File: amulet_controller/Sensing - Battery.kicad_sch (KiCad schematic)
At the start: 3 parts

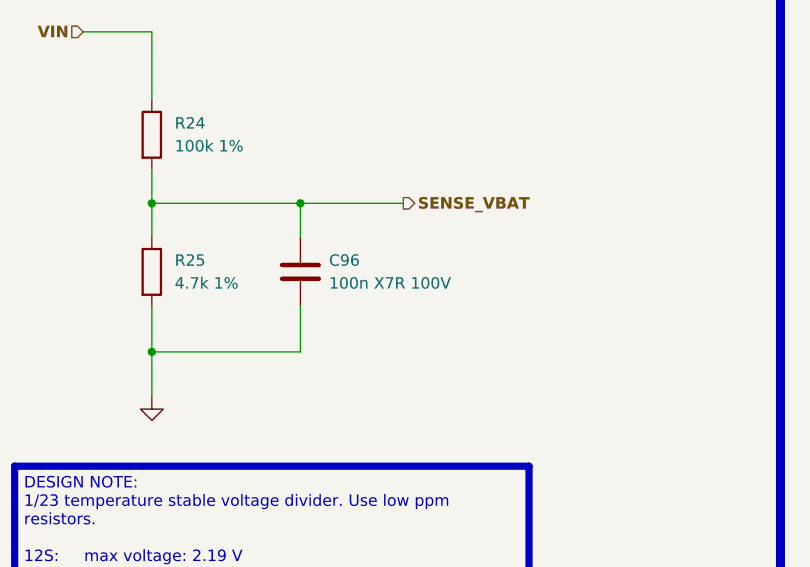
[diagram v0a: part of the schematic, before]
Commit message: filled in fields for bom, replaced inexisting components. Need to replace LEDs
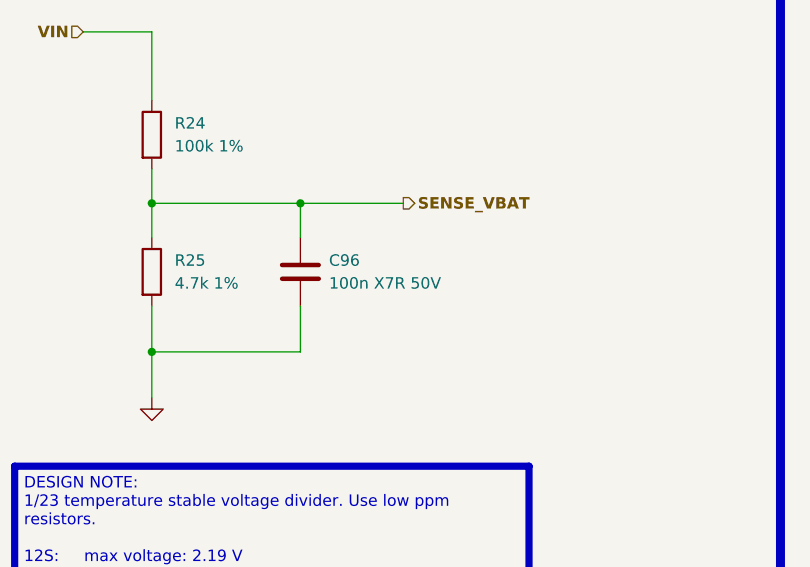
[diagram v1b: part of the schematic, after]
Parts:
- C96: value 100n X7R 100V -> 100n X7R 50V; Manufacturer (none) -> Murata Electronics; Manufacturer Part Number (none) -> GCM155R71H104KE02J; Supplier 1 (none) -> Digikey; Supplier Part Number 1 (none) -> 490-14514-1-ND
- R24: Manufacturer (none) -> YAGEO; Manufacturer Part Number (none) -> RT0402FRE07100KL; Supplier 1 (none) -> Digikey; Supplier Part Number 1 (none) -> YAG2307CT-ND
- R25: Manufacturer (none) -> YAGEO; Manufacturer Part Number (none) -> RT0402FRE134K7L; Supplier 1 (none) -> Digikey; Supplier Part Number 1 (none) -> 13-RT0402FRE134K7LCT-ND
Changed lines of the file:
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@@
       (effects (font (size 1.27 1.27)) hide)
     )
-    (property "Datasheet" "~" (at 134.62 78.74 0)
+    (property "Datasheet" "https://www.yageo.com/upload/media/product/app/datasheet/rchip/pyu-rt_1-to-0.01_rohs_l.pdf" (at 134.62 78.74 0)
+      (effects (font (size 1.27 1.27)) hide)
+    )
+    (property "Description" "RES 4.7K OHM 1% 1/16W 0402 50PPM" (at 134.62 78.74 0)
+      (effects (font (size 1.27 1.27)) hide)
+    )
+    (property "Manufacturer" "YAGEO" (at 134.62 78.74 0)
+      (effects (font (size 1.27 1.27)) hide)
+    )
+    (property "Manufacturer Part Number" "RT0402FRE134K7L" (at 134.62 78.74 0)
+      (effects (font (size 1.27 1.27)) hide)
+    )
+    (property "Supplier 1" "Digikey" (at 134.62 78.74 0)
+      (effects (font (size 1.27 1.27)) hide)
+    )
+    (property "Supplier Part Number 1" "13-RT0402FRE134K7LCT-ND" (at 134.62 78.74 0)
       (effects (font (size 1.27 1.27)) hide)
     )
@@
     (pin "2")
     (instances
-      (project "bldc_controller"
+      (project "amulet_controller"
         (path "/0650c7a8-acba-429c-9f8e-eec0baf0bc1c/fede4c36-00cc-4d3d-b71c-5243ba232202/5af28e14-08f4-4265-bd51-d6e5daa4b8a2"
           (reference "R25") (unit 1)
@@
       (effects (font (size 1.27 1.27)) (justify left))
     )
-    (property "Value" "100n X7R 100V" (at 154.305 80.01 0)
+    (property "Value" "100n X7R 50V" (at 154.305 80.01 0)
       (effects (font (size 1.27 1.27)) (justify left))
     )
@@
       (effects (font (size 1.27 1.27)) hide)
     )
-    (property "Datasheet" "~" (at 151.13 78.74 0)
+    (property "Datasheet" "https://search.murata.co.jp/Ceramy/image/img/A01X/G101/ENG/GCM155R71H104KE02-01.pdf" (at 151.13 78.74 0)
+      (effects (font (size 1.27 1.27)) hide)
+    )
+    (property "Description" "0.1 µF ±10% 50V Ceramic Capacitor X7R 0402 (1005 Metric)" (at 151.13 78.74 0)
+      (effects (font (size 1.27 1.27)) hide)
+    )
+    (property "Manufacturer" "Murata Electronics" (at 151.13 78.74 0)
+      (effects (font (size 1.27 1.27)) hide)
+    )
+    (property "Manufacturer Part Number" "GCM155R71H104KE02J" (at 151.13 78.74 0)
+      (effects (font (size 1.27 1.27)) hide)
+    )
+    (property "Supplier 1" "Digikey" (at 151.13 78.74 0)
+      (effects (font (size 1.27 1.27)) hide)
+    )
+    (property "Supplier Part Number 1" "490-14514-1-ND" (at 151.13 78.74 0)
       (effects (font (size 1.27 1.27)) hide)
     )
@@
     (pin "2")
     (instances
-      (project "bldc_controller"
+      (project "amulet_controller"
         (path "/0650c7a8-acba-429c-9f8e-eec0baf0bc1c/fede4c36-00cc-4d3d-b71c-5243ba232202/5af28e14-08f4-4265-bd51-d6e5daa4b8a2"
           (reference "C96") (unit 1)
@@
     (pin "1")
     (instances
-      (project "bldc_controller"
+      (project "amulet_controller"
         (path "/0650c7a8-acba-429c-9f8e-eec0baf0bc1c/fede4c36-00cc-4d3d-b71c-5243ba232202/5af28e14-08f4-4265-bd51-d6e5daa4b8a2"
           (reference "#PWR044") (unit 1)
@@
       (effects (font (size 1.27 1.27)) hide)
     )
-    (property "Datasheet" "~" (at 134.62 63.5 0)
+    (property "Datasheet" "https://www.yageo.com/upload/media/product/app/datasheet/rchip/pyu-rt_1-to-0.01_rohs_l.pdf" (at 134.62 63.5 0)
+      (effects (font (size 1.27 1.27)) hide)
+    )
+    (property "Description" "RES SMD 100K OHM 1% 1/16W 0402" (at 134.62 63.5 0)
+      (effects (font (size 1.27 1.27)) hide)
+    )
+    (property "Manufacturer" "YAGEO" (at 134.62 63.5 0)
+      (effects (font (size 1.27 1.27)) hide)
+    )
+    (property "Manufacturer Part Number" "RT0402FRE07100KL" (at 134.62 63.5 0)
+      (effects (font (size 1.27 1.27)) hide)
+    )
+    (property "Supplier 1" "Digikey" (at 134.62 63.5 0)
+      (effects (font (size 1.27 1.27)) hide)
+    )
+    (property "Supplier Part Number 1" "YAG2307CT-ND" (at 134.62 63.5 0)
       (effects (font (size 1.27 1.27)) hide)
     )
@@
     (pin "2")
     (instances
-      (project "bldc_controller"
+      (project "amulet_controller"
         (path "/0650c7a8-acba-429c-9f8e-eec0baf0bc1c/fede4c36-00cc-4d3d-b71c-5243ba232202/5af28e14-08f4-4265-bd51-d6e5daa4b8a2"
           (reference "R24") (unit 1)

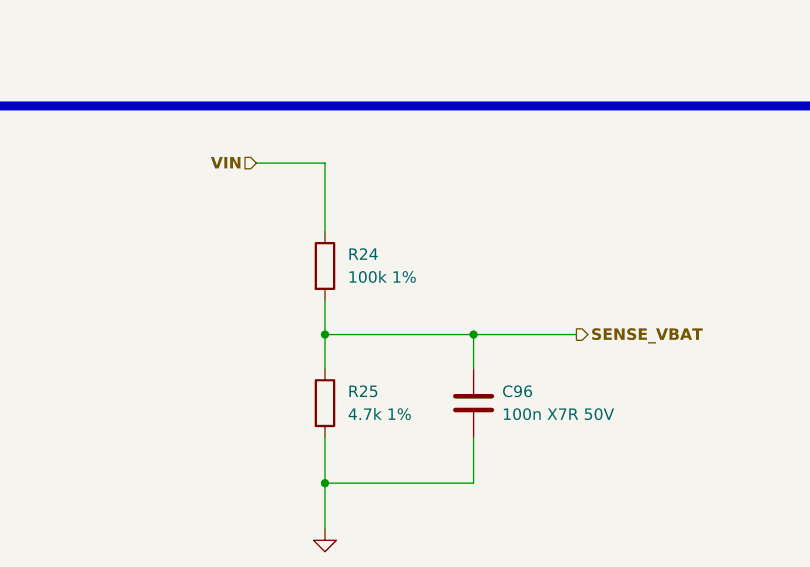
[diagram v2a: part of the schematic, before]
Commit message: finalized pcb. TODO: add clean BOM and KiBot integration
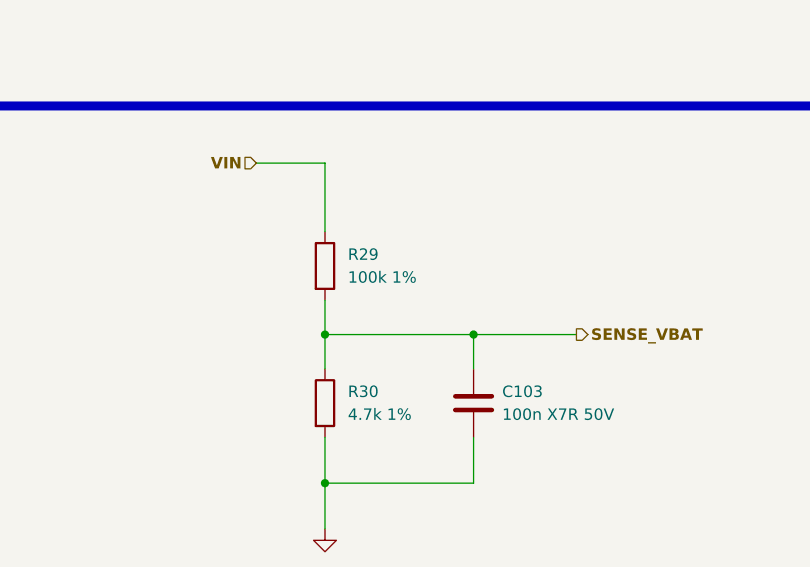
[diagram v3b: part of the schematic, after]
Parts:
- renumbered C96 to C103, R24 to R29, R25 to R30
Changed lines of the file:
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@@
+    (stroke (width 0) (type default))
+  )
+  (wire (pts (xy 134.62 59.69) (xy 134.62 52.07))
     (stroke (width 0) (type default))
   )
@@
     (stroke (width 0) (type default))
   )
-  (wire (pts (xy 134.62 52.07) (xy 134.62 59.69))
-    (stroke (width 0.381) (type default) (color 200 50 50 1))
+  (wire (pts (xy 151.13 71.12) (xy 162.56 71.12))
+    (stroke (width 0) (type default))
   )
-  (wire (pts (xy 151.13 71.12) (xy 162.56 71.12))
+  (wire (pts (xy 134.62 52.07) (xy 127 52.07))
     (stroke (width 0) (type default))
   )
   (wire (pts (xy 134.62 67.31) (xy 134.62 71.12))
     (stroke (width 0) (type default))
-  )
-  (wire (pts (xy 127 52.07) (xy 134.62 52.07))
-    (stroke (width 0.381) (type default) (color 200 50 50 1))
   )
   (wire (pts (xy 134.62 92.71) (xy 134.62 87.63))
@@
   )
   (hierarchical_label "VIN" (shape input) (at 127 52.07 180) (fields_autoplaced)
-    (effects (font (face "Arial") (size 1.27 1.27) bold) (justify right))
+    (effects (font (face "Arial") (size 1.27 1.27) bold (color 0 0 0 1)) (justify right))
   )
   (hierarchical_label "SENSE_VBAT" (shape output) (at 162.56 71.12 0) (fields_autoplaced)
@@
   (symbol (lib_id "Device:R") (at 134.62 78.74 0) (unit 1)
     (in_bom yes) (on_board yes) (dnp no) (fields_autoplaced)
-    (property "Reference" "R25" (at 137.16 77.47 0)
+    (property "Reference" "R30" (at 137.16 77.47 0)
       (effects (font (size 1.27 1.27)) (justify left))
     )
@@
       (project "amulet_controller"
         (path "/0650c7a8-acba-429c-9f8e-eec0baf0bc1c/fede4c36-00cc-4d3d-b71c-5243ba232202/5af28e14-08f4-4265-bd51-d6e5daa4b8a2"
-          (reference "R25") (unit 1)
+          (reference "R30") (unit 1)
         )
       )
@@
   (symbol (lib_id "Device:C") (at 151.13 78.74 0) (unit 1)
     (in_bom yes) (on_board yes) (dnp no) (fields_autoplaced)
-    (property "Reference" "C96" (at 154.305 77.47 0)
+    (property "Reference" "C103" (at 154.305 77.47 0)
       (effects (font (size 1.27 1.27)) (justify left))
     )
@@
       (project "amulet_controller"
         (path "/0650c7a8-acba-429c-9f8e-eec0baf0bc1c/fede4c36-00cc-4d3d-b71c-5243ba232202/5af28e14-08f4-4265-bd51-d6e5daa4b8a2"
-          (reference "C96") (unit 1)
+          (reference "C103") (unit 1)
         )
       )
@@
   (symbol (lib_id "power:GND") (at 134.62 92.71 0) (unit 1)
     (in_bom yes) (on_board yes) (dnp no) (fields_autoplaced)
-    (property "Reference" "#PWR044" (at 134.62 99.06 0)
+    (property "Reference" "#PWR045" (at 134.62 99.06 0)
       (effects (font (size 1.27 1.27)) hide)
     )
@@
       (project "amulet_controller"
         (path "/0650c7a8-acba-429c-9f8e-eec0baf0bc1c/fede4c36-00cc-4d3d-b71c-5243ba232202/5af28e14-08f4-4265-bd51-d6e5daa4b8a2"
-          (reference "#PWR044") (unit 1)
+          (reference "#PWR045") (unit 1)
         )
       )
@@
   (symbol (lib_id "Device:R") (at 134.62 63.5 0) (unit 1)
     (in_bom yes) (on_board yes) (dnp no) (fields_autoplaced)
-    (property "Reference" "R24" (at 137.16 62.23 0)
+    (property "Reference" "R29" (at 137.16 62.23 0)
       (effects (font (size 1.27 1.27)) (justify left))
     )
@@
       (project "amulet_controller"
         (path "/0650c7a8-acba-429c-9f8e-eec0baf0bc1c/fede4c36-00cc-4d3d-b71c-5243ba232202/5af28e14-08f4-4265-bd51-d6e5daa4b8a2"
-          (reference "R24") (unit 1)
+          (reference "R29") (unit 1)
         )
       )

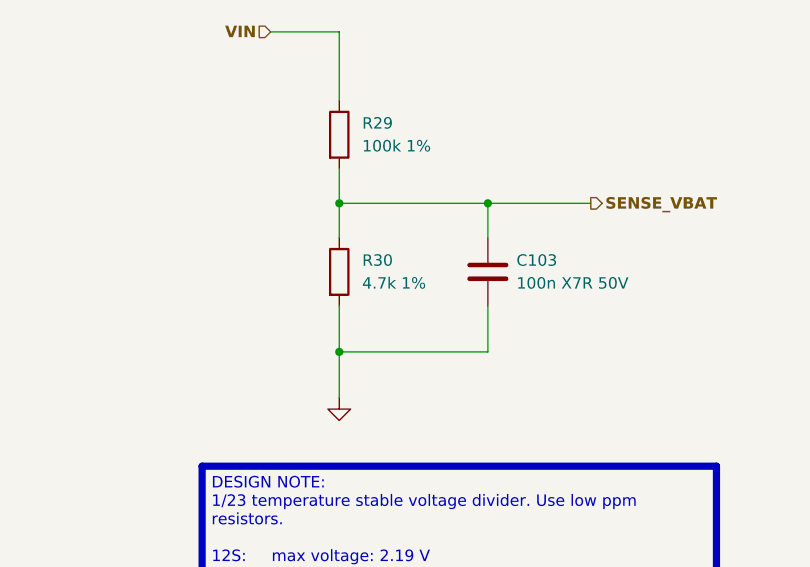
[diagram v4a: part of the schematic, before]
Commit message: Fixed clearance between +VBAT via and GND
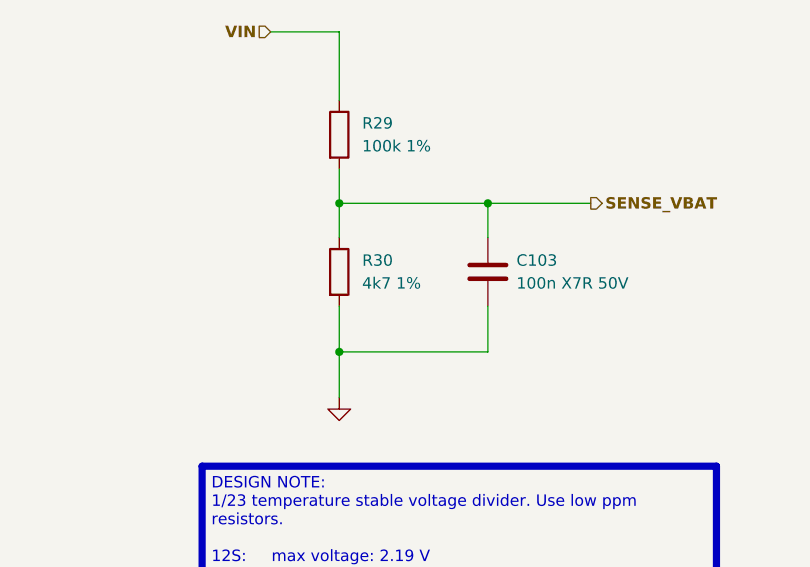
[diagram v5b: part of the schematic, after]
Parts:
- R30: value 4.7k 1% -> 4k7 1%
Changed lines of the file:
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@@
       (effects (font (size 1.27 1.27)) (justify left))
     )
-    (property "Value" "4.7k 1%" (at 137.16 80.01 0)
+    (property "Value" "4k7 1%" (at 137.16 80.01 0)
       (effects (font (size 1.27 1.27)) (justify left))
     )
